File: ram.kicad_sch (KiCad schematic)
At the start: 56 parts

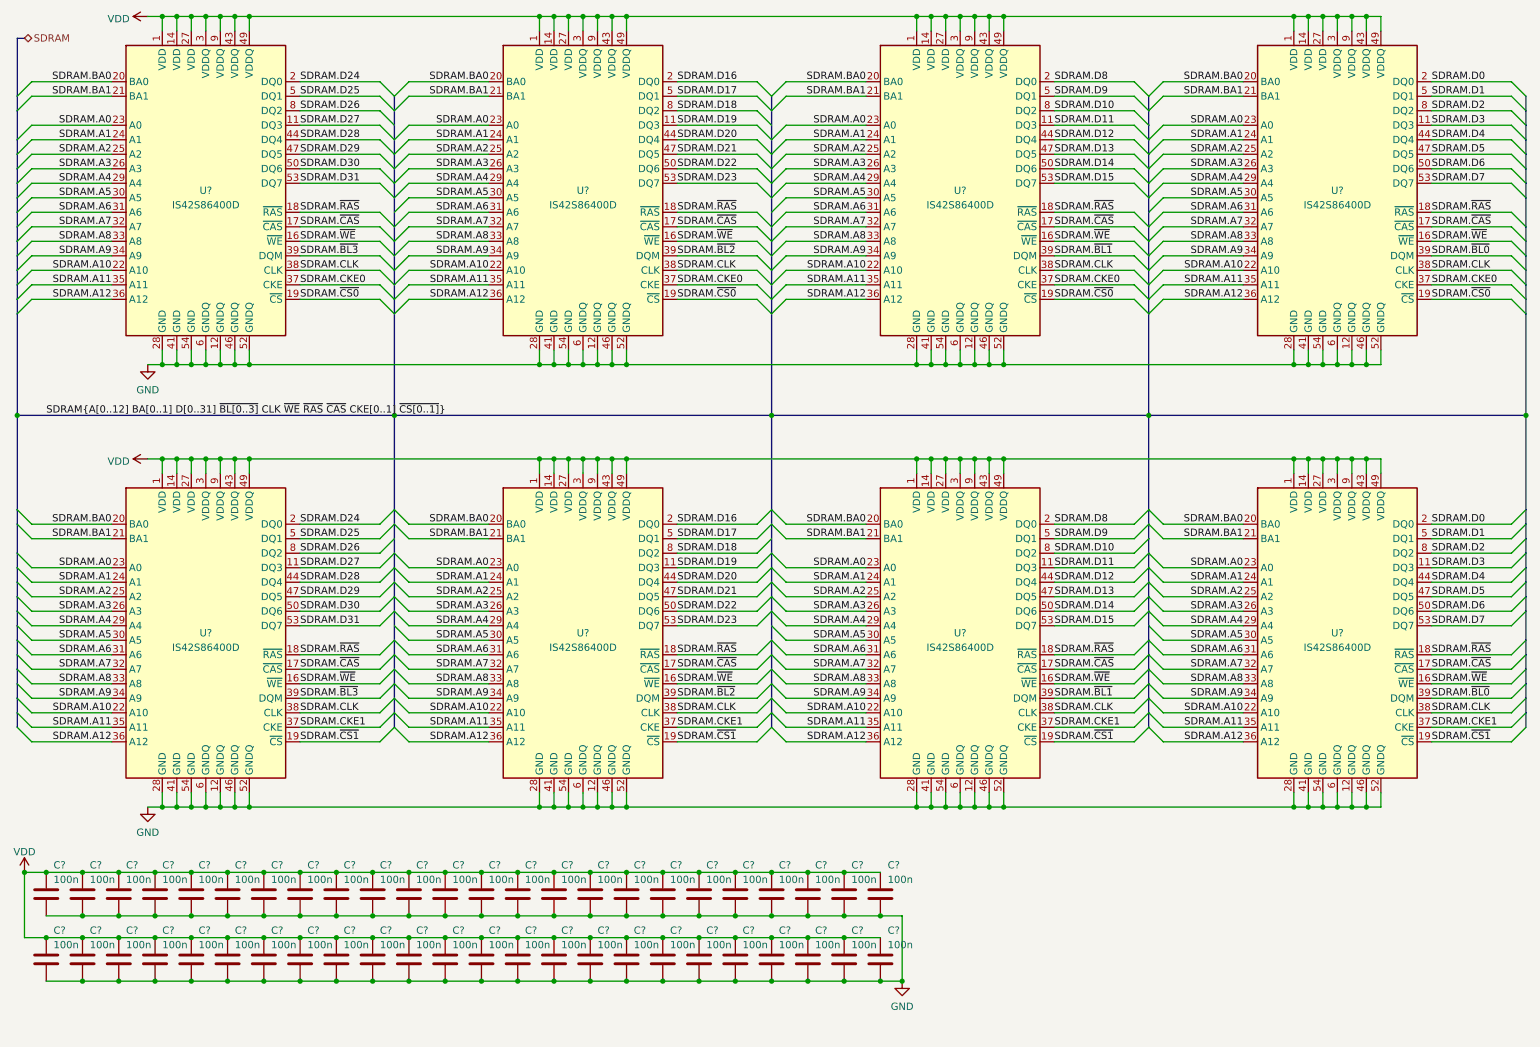
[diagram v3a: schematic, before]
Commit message: Capacitor part assignment
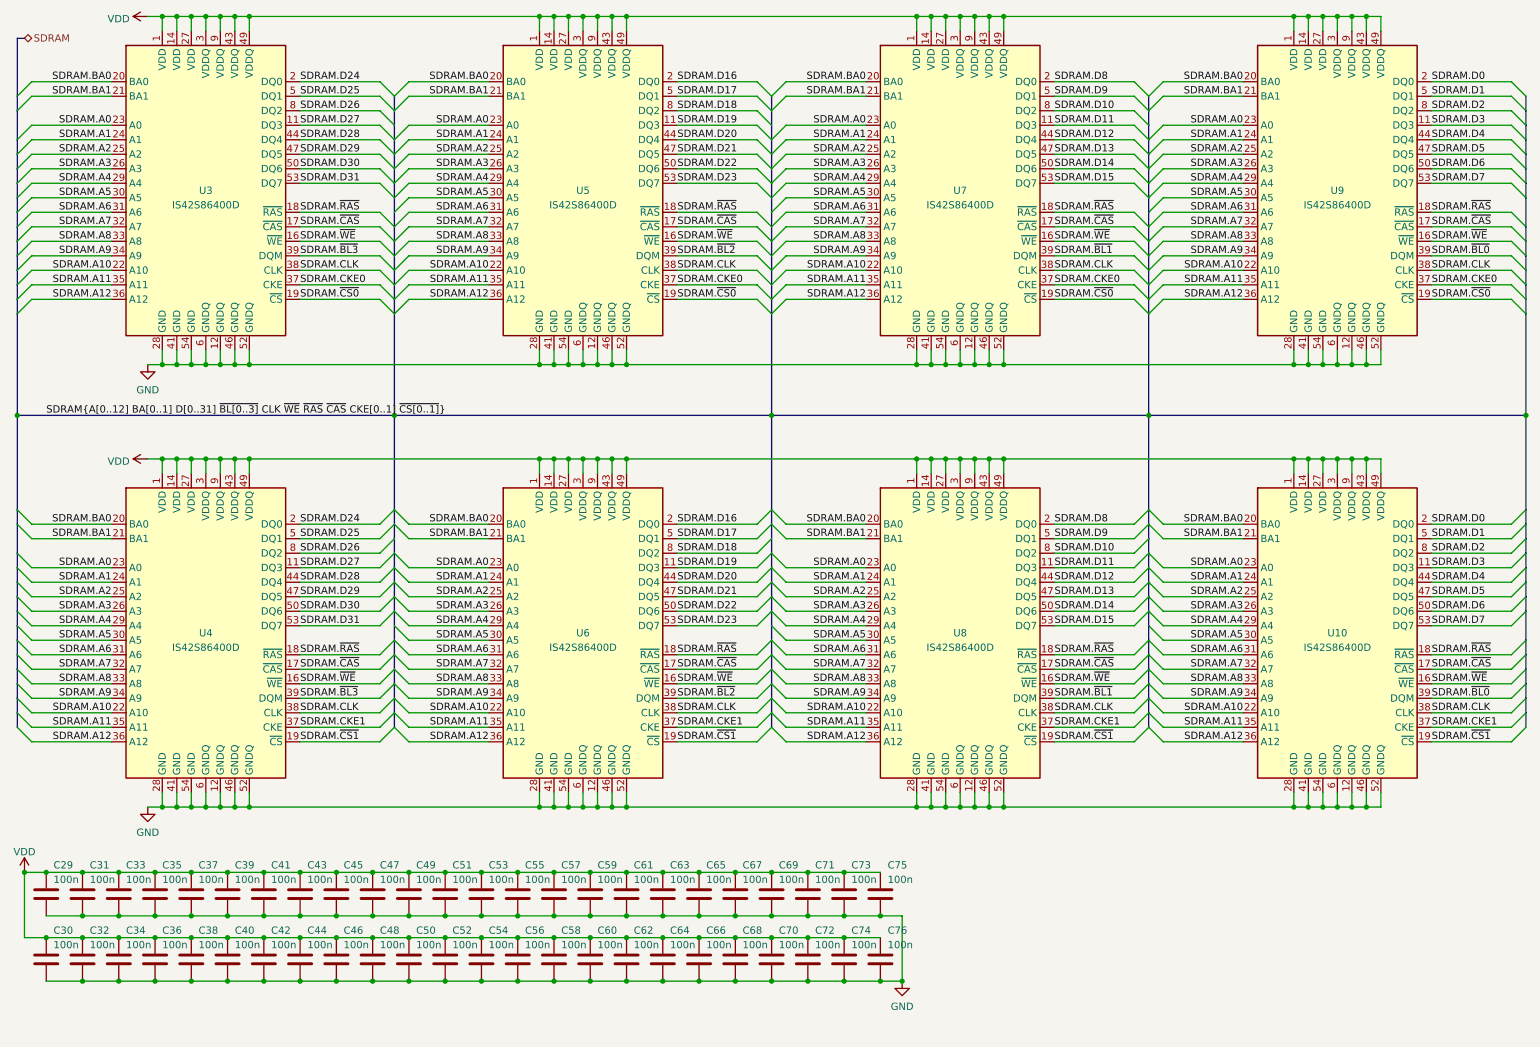
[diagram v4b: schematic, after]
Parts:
- gave numbers to parts that had none: 56

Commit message: Final annotate pass
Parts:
- renumbered C29 to C401, C30 to C402, C31 to C403, C32 to C404, C33 to C405, C34 to C406, C35 to C407, C36 to C408, C37 to C409, C38 to C410, C39 to C411, C40 to C412, C41 to C413, C42 to C414, C43 to C415, C44 to C416, C45 to C417, C46 to C418, C47 to C419, C48 to C420, C49 to C421, C50 to C422, C51 to C423, C52 to C424, C53 to C425, C54 to C426, C55 to C427, C56 to C428, C57 to C429, C58 to C430, C59 to C431, C60 to C432, C61 to C433, C62 to C434, C63 to C435, C64 to C436, C65 to C437, C66 to C438, C67 to C439, C68 to C440, C69 to C441, C70 to C442, C71 to C443, C72 to C444, C73 to C445, C74 to C446, C75 to C447, C76 to C448, U3 to U401, U4 to U402, U5 to U403, U6 to U404, U7 to U405, U8 to U406, U9 to U407, U10 to U408

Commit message: Fix overlapped label on DRAM data bus causing D16 and D18 nets to be connected together.
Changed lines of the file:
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@@
     (stroke (width 0) (type default) (color 0 0 0 0))
   )
+  (bus_entry (at 148.59 34.29) (size -2.54 -2.54)
+    (stroke (width 0) (type default) (color 0 0 0 0))
+  )
   (bus_entry (at 146.05 124.46) (size 2.54 -2.54)
     (stroke (width 0) (type default) (color 0 0 0 0))
@@
     (stroke (width 0) (type default) (color 0 0 0 0))
   )
-  (bus_entry (at 148.59 34.29) (size -2.54 -2.54)
-    (stroke (width 0) (type default) (color 0 0 0 0))
-  )
   (bus_entry (at 278.13 111.76) (size 2.54 -2.54)
     (stroke (width 0) (type default) (color 0 0 0 0))
@@
     (stroke (width 0) (type default) (color 0 0 0 0))
   )
-  (bus_entry (at 146.05 109.22) (size 2.54 -2.54)
-    (stroke (width 0) (type default) (color 0 0 0 0))
-  )
   (bus_entry (at 148.59 142.24) (size 2.54 2.54)
     (stroke (width 0) (type default) (color 0 0 0 0))
@@
     (stroke (width 0) (type default) (color 0 0 0 0))
   )
+  (bus_entry (at 148.59 106.68) (size -2.54 2.54)
+    (stroke (width 0) (type default) (color 0 0 0 0))
+  )
   (bus_entry (at 280.67 52.07) (size -2.54 -2.54)
     (stroke (width 0) (type default) (color 0 0 0 0))
@@
     (stroke (width 0) (type default) (color 0 0 0 0))
   )
-  (wire (pts (xy 132.08 109.22) (xy 146.05 109.22))
-    (stroke (width 0) (type default) (color 0 0 0 0))
-  )
   (wire (pts (xy 129.54 170.18) (xy 135.89 170.18))
     (stroke (width 0) (type default) (color 0 0 0 0))
@@
     (stroke (width 0) (type default) (color 0 0 0 0))
   )
+  (wire (pts (xy 132.08 109.22) (xy 146.05 109.22))
+    (stroke (width 0) (type default) (color 0 0 0 0))
+  )
   (wire (pts (xy 132.08 64.77) (xy 146.05 64.77))
     (stroke (width 0) (type default) (color 0 0 0 0))
@@
     (stroke (width 0) (type default) (color 0 0 0 0))
   )
+  (wire (pts (xy 132.08 31.75) (xy 146.05 31.75))
+    (stroke (width 0) (type default) (color 0 0 0 0))
+  )
   (wire (pts (xy 85.09 31.75) (xy 99.06 31.75))
     (stroke (width 0) (type default) (color 0 0 0 0))
@@
     (stroke (width 0) (type default) (color 0 0 0 0))
   )
-  (wire (pts (xy 132.08 31.75) (xy 146.05 31.75))
-    (stroke (width 0) (type default) (color 0 0 0 0))
-  )
   (wire (pts (xy 39.37 81.28) (xy 41.91 81.28))
     (stroke (width 0) (type default) (color 0 0 0 0))
@@
     (effects (font (size 1.27 1.27)) (justify right bottom))
   )
+  (label "SDRAM.D16" (at 132.08 31.75 0)
+    (effects (font (size 1.27 1.27)) (justify left bottom))
+  )
   (label "SDRAM.A6" (at 99.06 132.08 180)
     (effects (font (size 1.27 1.27)) (justify right bottom))
@@
     (effects (font (size 1.27 1.27)) (justify right bottom))
   )
-  (label "SDRAM.D16" (at 132.08 109.22 0)
-    (effects (font (size 1.27 1.27)) (justify left bottom))
-  )
   (label "SDRAM.BA1" (at 231.14 111.76 180)
     (effects (font (size 1.27 1.27)) (justify right bottom))
@@
     (effects (font (size 1.27 1.27)) (justify right bottom))
   )
+  (label "SDRAM.D16" (at 132.08 109.22 0)
+    (effects (font (size 1.27 1.27)) (justify left bottom))
+  )
   (label "SDRAM.~{RAS}" (at 66.04 132.08 0)
     (effects (font (size 1.27 1.27)) (justify left bottom))
@@
     (effects (font (size 1.27 1.27)) (justify left bottom))
   )
-  (label "SDRAM.D16" (at 132.08 31.75 0)
-    (effects (font (size 1.27 1.27)) (justify left bottom))
-  )

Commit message: Add worksheet template with PoliMi logo.
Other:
- title: (none) -> MARCO RAM Board
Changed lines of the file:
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@@
 (kicad_sch (version 20211123) (generator eeschema)
   (paper "A4")
+  (title_block
+    (title "MARCO RAM Board")
+    (rev "1")
+    (comment 9 "SDRAM")
+  )
   (junction (at 173.99 81.28) (diameter 0) (color 0 0 0 0)
   )
